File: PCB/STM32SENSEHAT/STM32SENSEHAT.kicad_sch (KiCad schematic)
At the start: 0 parts

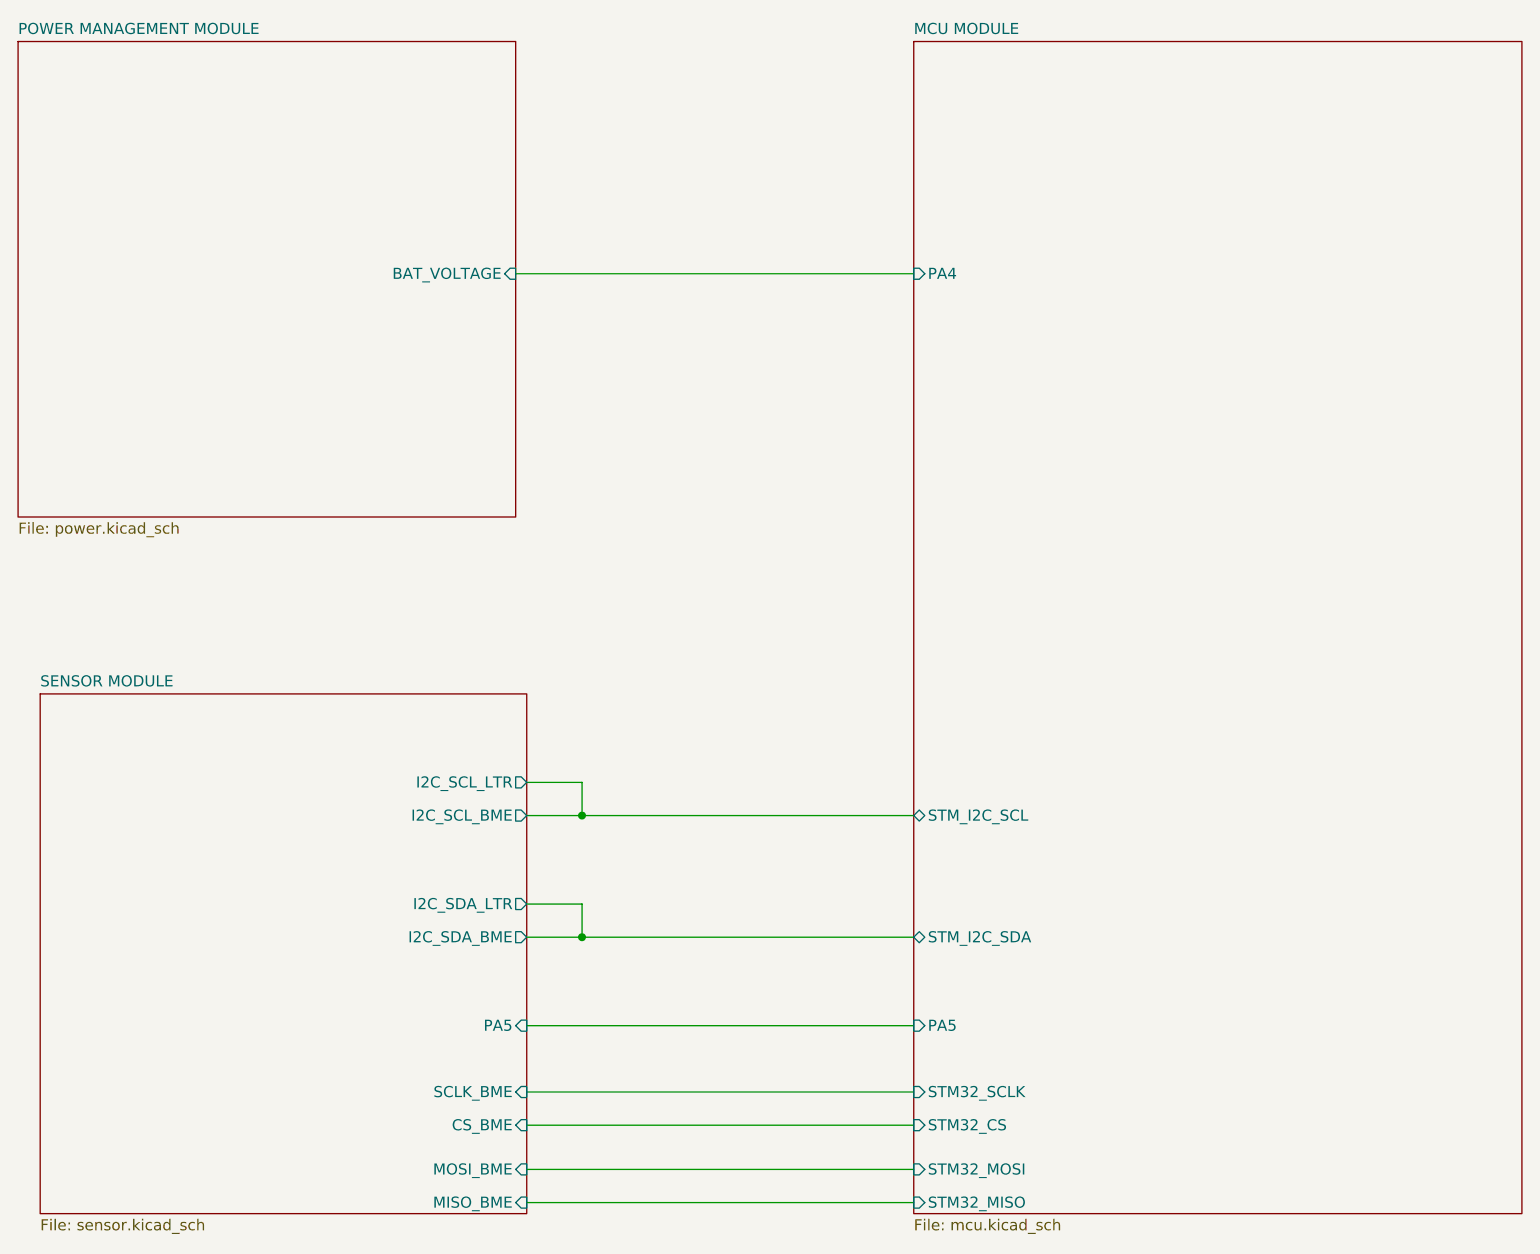
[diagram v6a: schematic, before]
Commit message: Rework of Power,MCU and Sensor Schematic
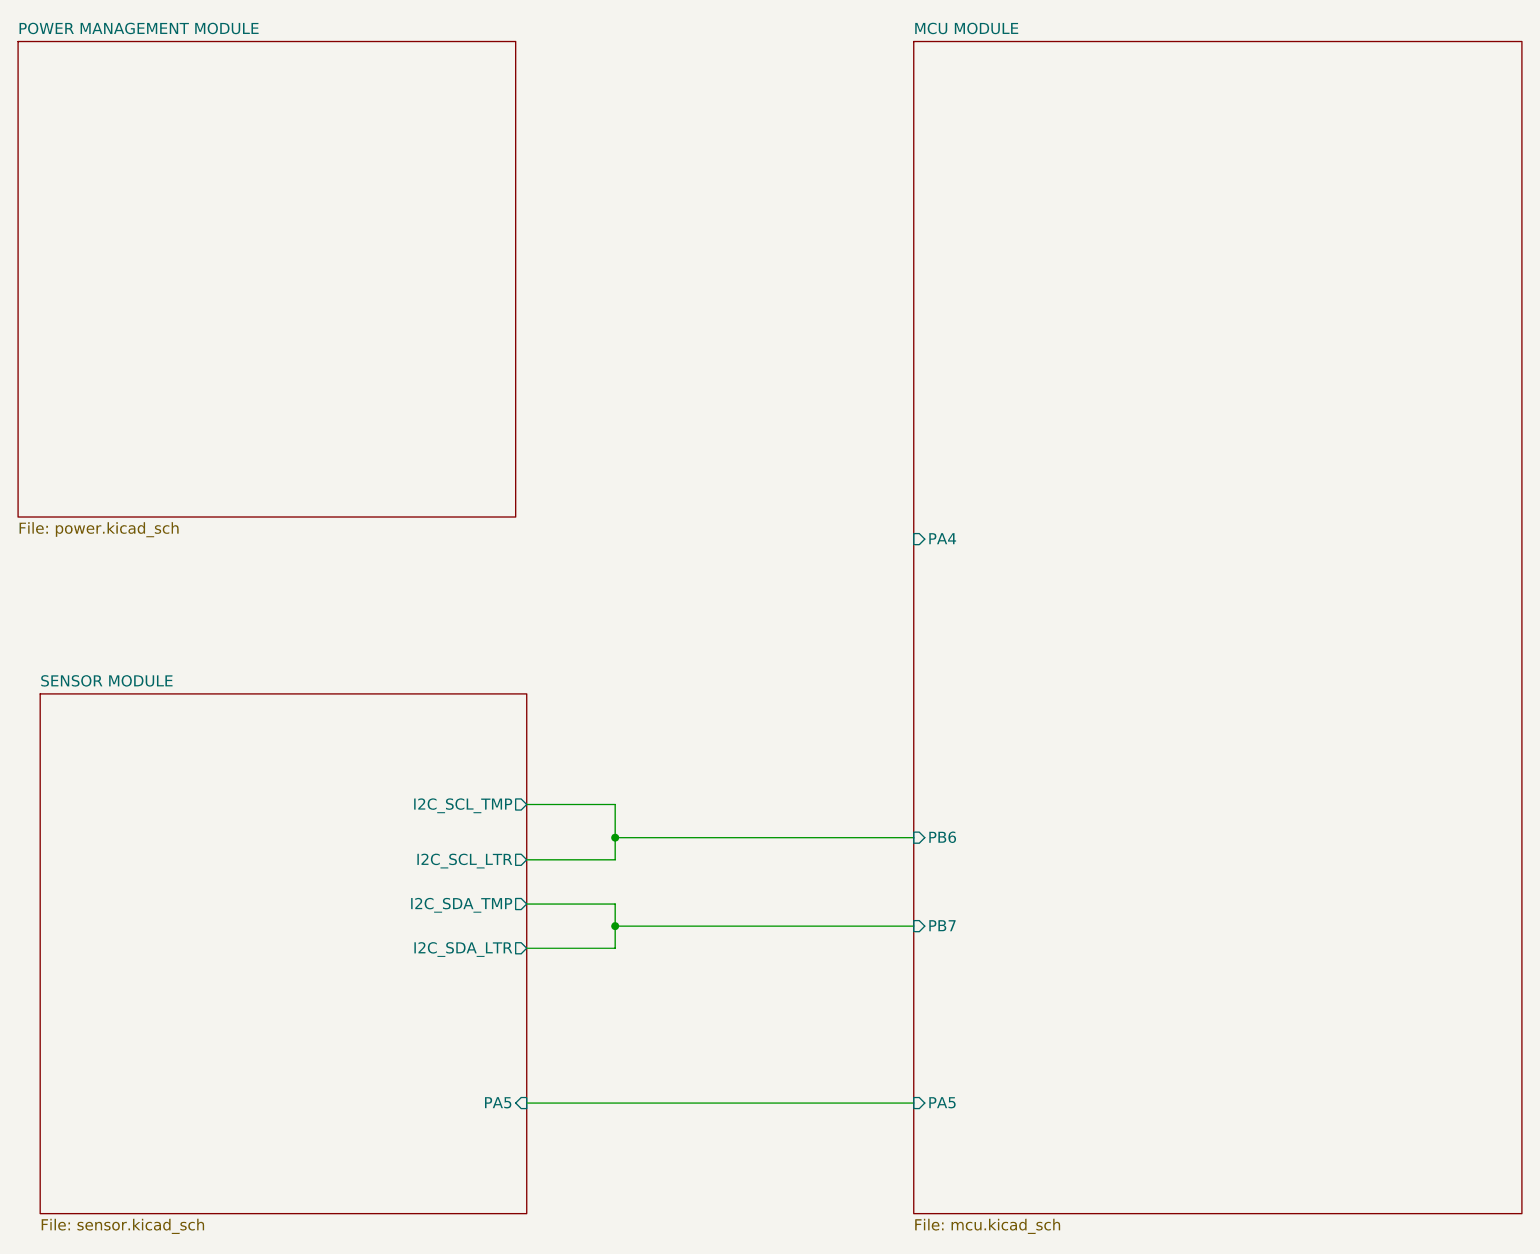
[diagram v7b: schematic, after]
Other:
- sheet MCU MODULE ports: added PB6, PB7; removed STM32_CS, STM32_MISO, STM32_MOSI, STM32_SCLK, STM_I2C_SCL, STM_I2C_SDA
- sheet POWER MANAGEMENT MODULE ports: added none; removed BAT_VOLTAGE
- sheet SENSOR MODULE ports: added I2C_SCL_TMP, I2C_SDA_TMP; removed CS_BME, I2C_SCL_BME, I2C_SDA_BME, MISO_BME, MOSI_BME, SCLK_BME
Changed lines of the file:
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@@
     (comment 4 "AUTHOR(S)")
   )
-  (junction (at 99.06 125.73) (diameter 0) (color 0 0 0 0)
-  )
-  (junction (at 99.06 111.76) (diameter 0) (color 0 0 0 0)
-  )
-  (wire (pts (xy 92.71 107.95) (xy 99.06 107.95))
-    (stroke (width 0) (type default))
-  )
-  (wire (pts (xy 99.06 111.76) (xy 137.16 111.76))
-    (stroke (width 0) (type default))
-  )
-  (wire (pts (xy 92.71 147.32) (xy 137.16 147.32))
-    (stroke (width 0) (type default))
-  )
-  (wire (pts (xy 99.06 107.95) (xy 99.06 111.76))
-    (stroke (width 0) (type default))
-  )
-  (wire (pts (xy 92.71 125.73) (xy 99.06 125.73))
-    (stroke (width 0) (type default))
-  )
-  (wire (pts (xy 99.06 121.92) (xy 99.06 125.73))
-    (stroke (width 0) (type default))
-  )
-  (wire (pts (xy 92.71 156.21) (xy 137.16 156.21))
-    (stroke (width 0) (type default))
-  )
-  (wire (pts (xy 91.44 49.53) (xy 137.16 49.53))
-    (stroke (width 0) (type default))
-  )
-  (wire (pts (xy 92.71 111.76) (xy 99.06 111.76))
-    (stroke (width 0) (type default))
-  )
-  (wire (pts (xy 92.71 143.51) (xy 137.16 143.51))
-    (stroke (width 0) (type default))
-  )
-  (wire (pts (xy 99.06 125.73) (xy 137.16 125.73))
-    (stroke (width 0) (type default))
-  )
-  (wire (pts (xy 92.71 121.92) (xy 99.06 121.92))
-    (stroke (width 0) (type default))
-  )
-  (wire (pts (xy 92.71 135.89) (xy 137.16 135.89))
-    (stroke (width 0) (type default))
-  )
-  (wire (pts (xy 92.71 152.4) (xy 137.16 152.4))
+  (junction (at 102.87 124.46) (diameter 0) (color 0 0 0 0)
+  )
+  (junction (at 102.87 114.3) (diameter 0) (color 0 0 0 0)
+  )
+  (wire (pts (xy 102.87 124.46) (xy 137.16 124.46))
+    (stroke (width 0) (type default))
+  )
+  (wire (pts (xy 92.71 110.49) (xy 102.87 110.49))
+    (stroke (width 0) (type default))
+  )
+  (wire (pts (xy 102.87 114.3) (xy 137.16 114.3))
+    (stroke (width 0) (type default))
+  )
+  (wire (pts (xy 92.71 144.78) (xy 137.16 144.78))
+    (stroke (width 0) (type default))
+  )
+  (wire (pts (xy 92.71 121.92) (xy 102.87 121.92))
+    (stroke (width 0) (type default))
+  )
+  (wire (pts (xy 102.87 116.84) (xy 92.71 116.84))
+    (stroke (width 0) (type default))
+  )
+  (wire (pts (xy 102.87 124.46) (xy 102.87 127))
+    (stroke (width 0) (type default))
+  )
+  (wire (pts (xy 102.87 127) (xy 92.71 127))
+    (stroke (width 0) (type default))
+  )
+  (wire (pts (xy 102.87 114.3) (xy 102.87 116.84))
+    (stroke (width 0) (type default))
+  )
+  (wire (pts (xy 102.87 121.92) (xy 102.87 124.46))
+    (stroke (width 0) (type default))
+  )
+  (wire (pts (xy 102.87 110.49) (xy 102.87 114.3))
     (stroke (width 0) (type default))
   )
@@
       (effects (font (size 1.27 1.27)) (justify left top))
     )
-    (pin "PA5" input (at 92.71 135.89 0)
+    (pin "I2C_SCL_TMP" output (at 92.71 110.49 0)
       (effects (font (size 1.27 1.27)) (justify right))
     )
-    (pin "I2C_SDA_BME" output (at 92.71 125.73 0)
+    (pin "I2C_SDA_TMP" output (at 92.71 121.92 0)
       (effects (font (size 1.27 1.27)) (justify right))
     )
-    (pin "I2C_SCL_BME" output (at 92.71 111.76 0)
+    (pin "PA5" input (at 92.71 144.78 0)
       (effects (font (size 1.27 1.27)) (justify right))
     )
-    (pin "I2C_SCL_LTR" output (at 92.71 107.95 0)
+    (pin "I2C_SDA_LTR" output (at 92.71 127 0)
       (effects (font (size 1.27 1.27)) (justify right))
     )
-    (pin "I2C_SDA_LTR" output (at 92.71 121.92 0)
-      (effects (font (size 1.27 1.27)) (justify right))
-    )
-    (pin "SCLK_BME" input (at 92.71 143.51 0)
-      (effects (font (size 1.27 1.27)) (justify right))
-    )
-    (pin "MISO_BME" input (at 92.71 156.21 0)
-      (effects (font (size 1.27 1.27)) (justify right))
-    )
-    (pin "CS_BME" input (at 92.71 147.32 0)
-      (effects (font (size 1.27 1.27)) (justify right))
-    )
-    (pin "MOSI_BME" input (at 92.71 152.4 0)
+    (pin "I2C_SCL_LTR" output (at 92.71 116.84 0)
       (effects (font (size 1.27 1.27)) (justify right))
     )
@@
       (effects (font (size 1.27 1.27)) (justify left top))
     )
-    (pin "STM_I2C_SDA" bidirectional (at 137.16 125.73 180)
+    (pin "PA4" input (at 137.16 80.01 180)
       (effects (font (size 1.27 1.27)) (justify left))
     )
-    (pin "PA5" input (at 137.16 135.89 180)
+    (pin "PA5" input (at 137.16 144.78 180)
       (effects (font (size 1.27 1.27)) (justify left))
     )
-    (pin "STM_I2C_SCL" bidirectional (at 137.16 111.76 180)
+    (pin "PB7" input (at 137.16 124.46 180)
       (effects (font (size 1.27 1.27)) (justify left))
     )
-    (pin "PA4" input (at 137.16 49.53 180)
-      (effects (font (size 1.27 1.27) (color 72 0 72 1)) (justify left))
-    )
-    (pin "STM32_SCLK" input (at 137.16 143.51 180)
-      (effects (font (size 1.27 1.27)) (justify left))
-    )
-    (pin "STM32_CS" input (at 137.16 147.32 180)
-      (effects (font (size 1.27 1.27)) (justify left))
-    )
-    (pin "STM32_MOSI" input (at 137.16 152.4 180)
-      (effects (font (size 1.27 1.27)) (justify left))
-    )
-    (pin "STM32_MISO" input (at 137.16 156.21 180)
+    (pin "PB6" input (at 137.16 114.3 180)
       (effects (font (size 1.27 1.27)) (justify left))
     )
@@
       (effects (font (size 1.27 1.27)) (justify left top))
     )
-    (pin "BAT_VOLTAGE" input (at 91.44 49.53 0)
-      (effects (font (size 1.27 1.27)) (justify right))
-    )
     (instances
